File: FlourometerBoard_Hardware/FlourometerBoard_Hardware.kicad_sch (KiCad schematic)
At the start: 14 parts, among them J1 RJ45_LED_Shielded, J2 Conn_01x12_Pin, U1 Teensy4.1_DEV-16771, U2 OKI

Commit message: Boxed and Labeled Circuits
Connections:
- no-connect marks 5 -> 47
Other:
- note added: "Connectors"
- note added: "Ethernet"
- note added: "Hamamatsu Connections"
- note added: "LEDs"
- note added: "OKI"
- note added: "Teensy"
- moved on the sheet: C1, C2, C3, Conn1A, Conn1B, D1, D2, D3, J1, J2, R1, R2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

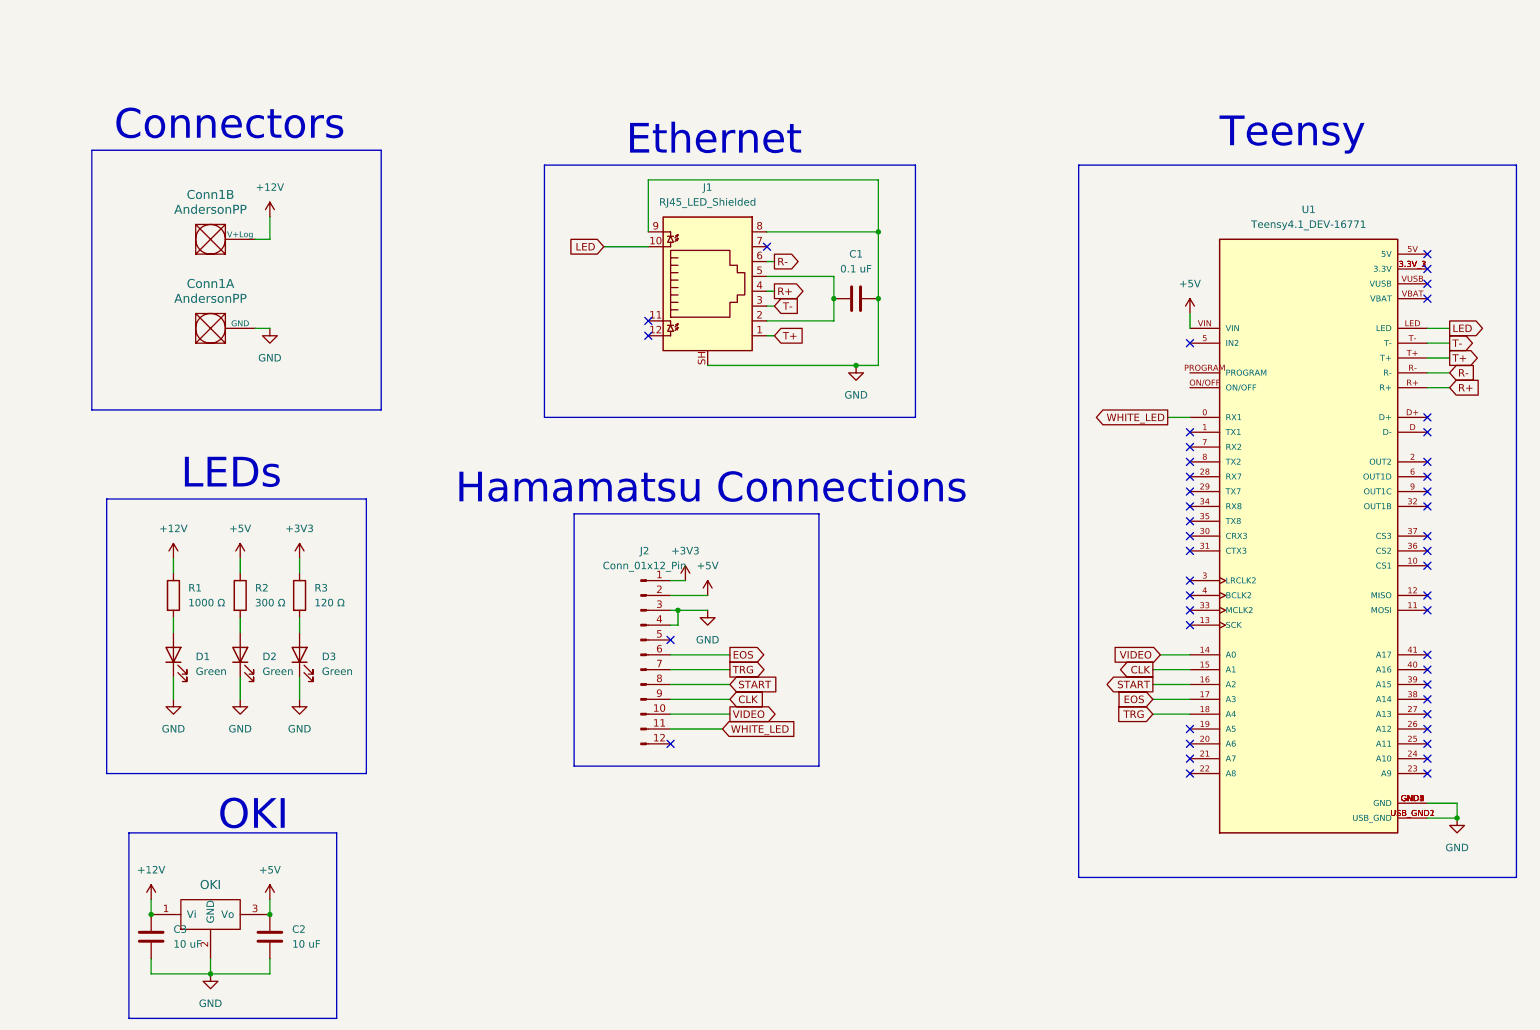
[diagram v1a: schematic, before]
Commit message: Update Board According to Schematic Review
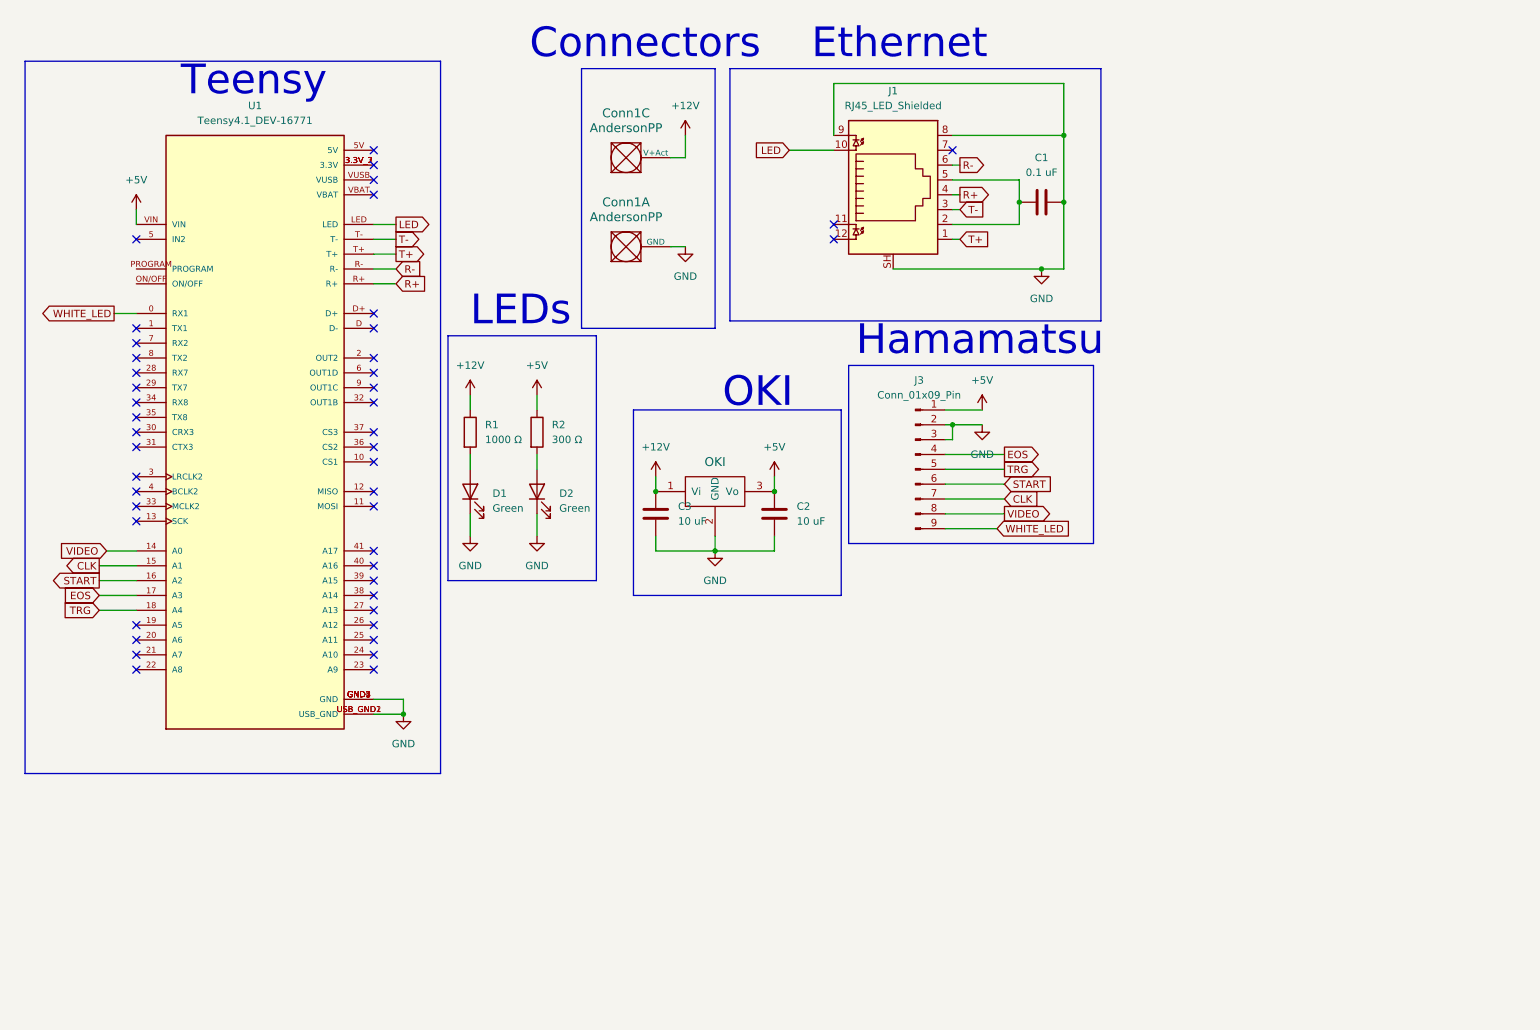
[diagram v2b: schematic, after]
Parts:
- removed unit 2 of Conn1
- removed D3: Green, symbol Device:LED
- removed J2: Conn_01x12_Pin, symbol Connector:Conn_01x12_Pin
- removed R3: 120 Ω, symbol Device:R
- added unit 3 of Conn1
- added J3: Conn_01x09_Pin, MRDT_Connectors:MOLEX_SL_09_Vertical, symbol Connector:Conn_01x09_Pin
- C1, C2, C3: footprint (none) -> Capacitor_SMD:C_0603_1608Metric_Pad1.08x0.95mm_HandSolder
- Conn1: footprint (none) -> MRDT_Connectors:Square_Anderson_2_H_Side_By_Side_PV
- D1, D2: footprint (none) -> LED_SMD:LED_0603_1608Metric_Pad1.05x0.95mm_HandSolder
- J1: footprint (none) -> MRDT_Connectors:RJ45_Teensy
- R1, R2: footprint (none) -> Resistor_SMD:R_0603_1608Metric_Pad0.98x0.95mm_HandSolder
- U1: footprint MODULE_DEV-16771 -> MRDT_Shields:Teensy_4_1_Ethernet
- U2: footprint (none) -> MRDT_Devices:OKI_Horizontal
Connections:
- net +12V: now also Conn1.3 (V+Act)
- net +5V: now also J3.1 (Pin_1)
- net CLK: now also J3.7 (Pin_7)
- net EOS: now also J3.4 (Pin_4)
- net GND: now also J3.2 (Pin_2), J3.3 (Pin_3)
- net START: now also J3.6 (Pin_6)
- net TRG: now also J3.5 (Pin_5)
- net VIDEO: now also J3.8 (Pin_8)
- net WHITE_LED: now also J3.9 (Pin_9)
- no-connect marks 47 -> 45
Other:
- note added: "Hamamatsu"
- note removed: "Hamamatsu Connections"
- moved on the sheet: C1, C2, C3, Conn1A, D1, D2, J1, R1, R2, U1

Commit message: Organized Schematic, Changed Anderson to V+Log
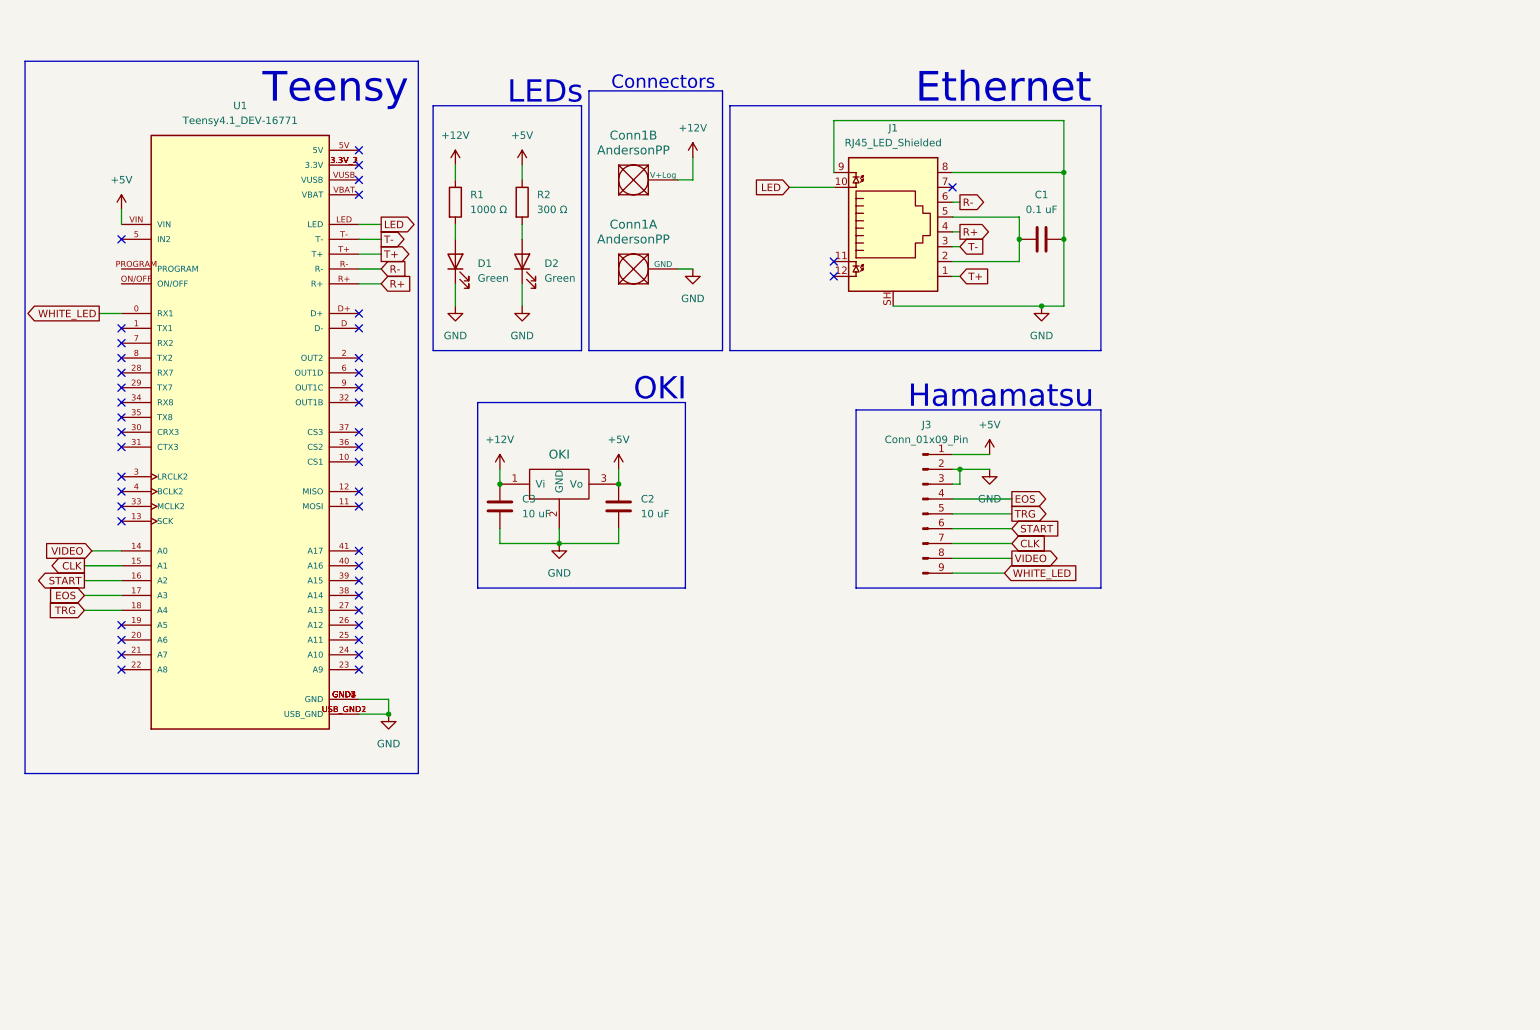
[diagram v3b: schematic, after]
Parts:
- removed unit 3 of Conn1
- added unit 2 of Conn1
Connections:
- net +12V: now also Conn1.2 (V+Log)
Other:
- moved on the sheet: C1, C2, C3, Conn1A, D1, D2, J1, J3, R1, R2, U1

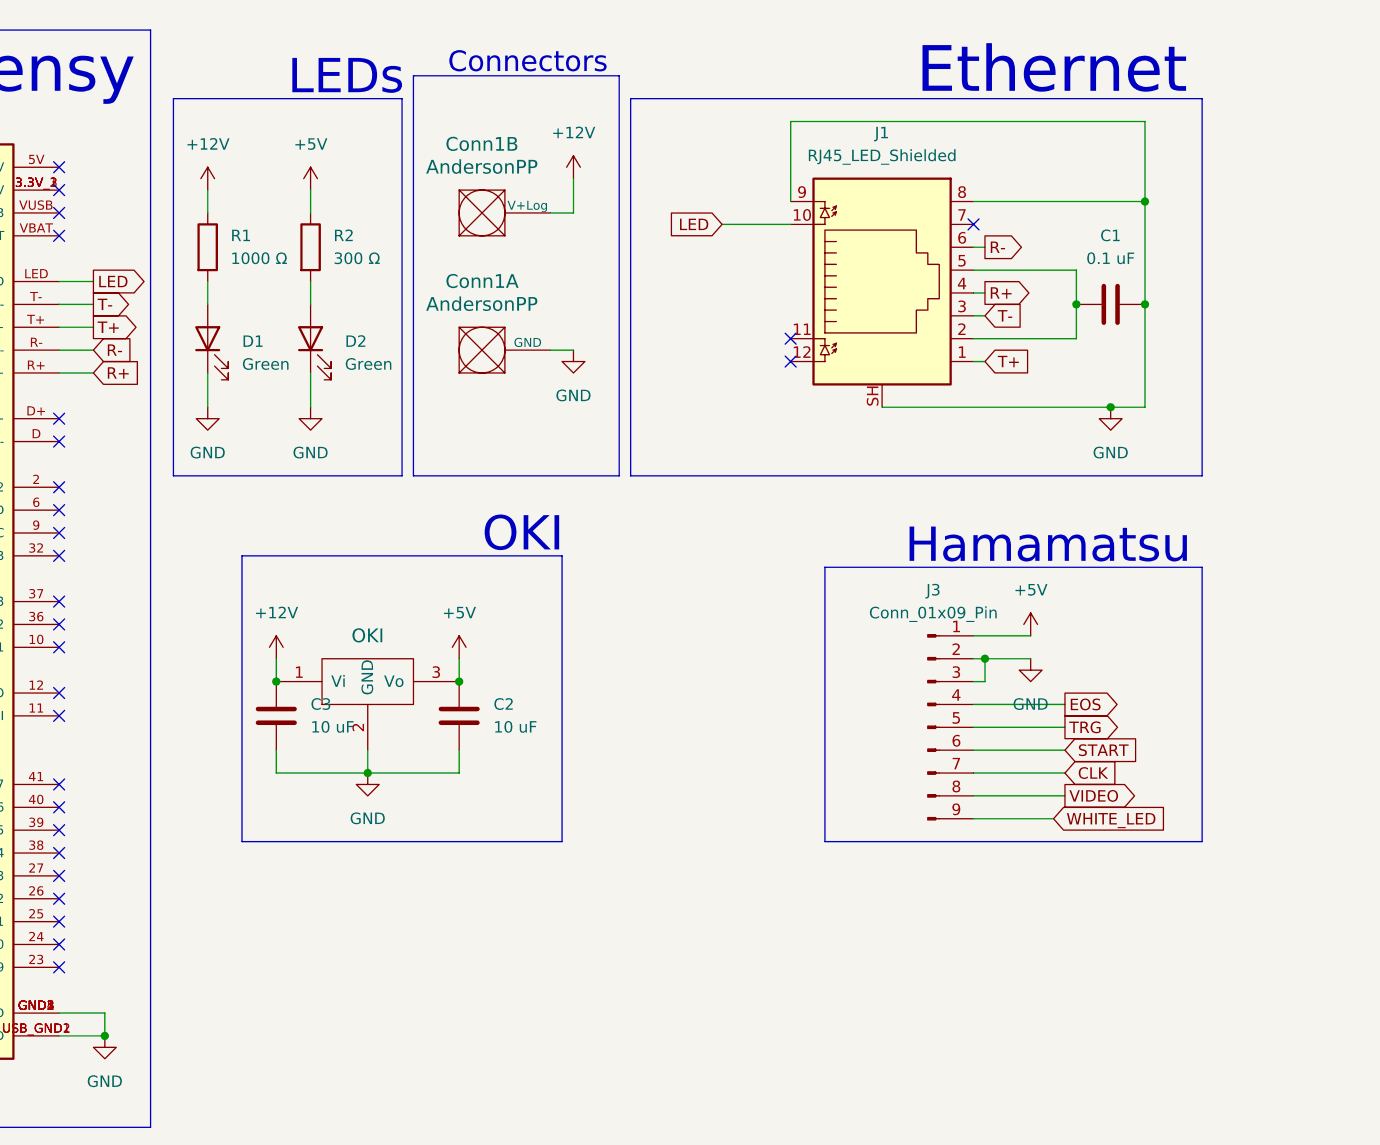
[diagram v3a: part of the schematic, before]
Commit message: Organized Schematic, added 12V to 3V3 converter
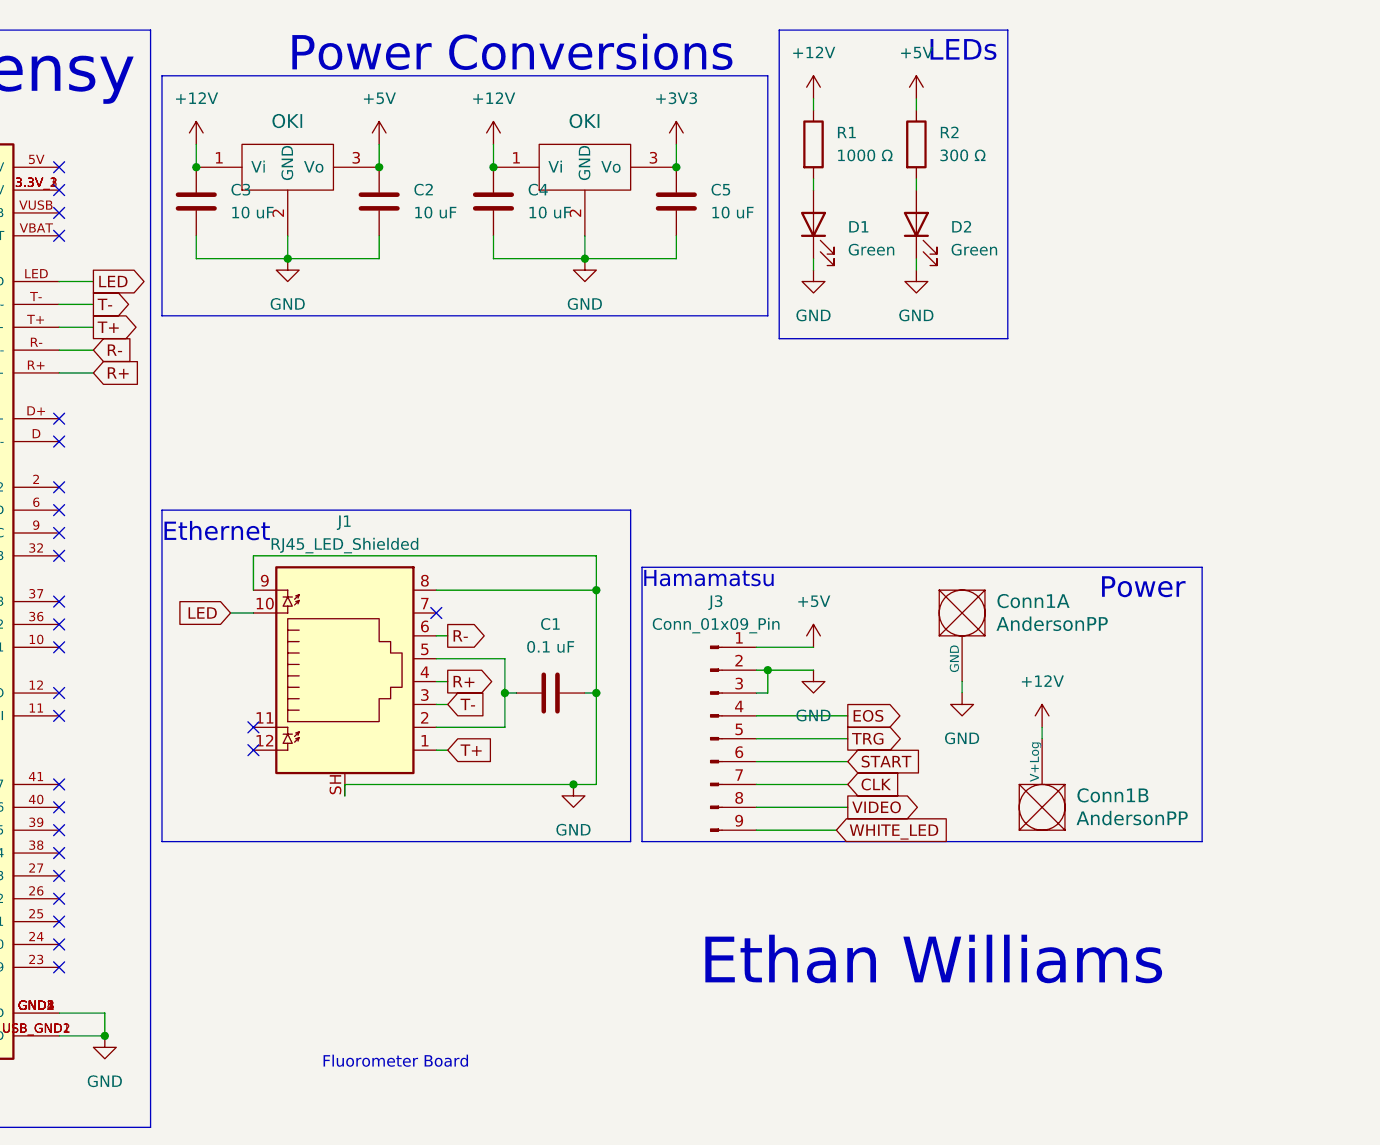
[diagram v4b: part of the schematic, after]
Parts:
- added C4, C5: 10 uF, Capacitor_SMD:C_0603_1608Metric_Pad1.08x0.95mm_HandSolder, symbol Device:C
- added U3: OKI, MRDT_Devices:OKI_Horizontal, symbol MRDT_Devices:OKI
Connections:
- net +12V: now also C4.1, U3.1 (Vi)
- net GND: now also C4.2, C5.2, U3.2 (GND)
- new net +3V3: C5.1, U3.3 (Vo)
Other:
- note added: "Ethan Williams"
- note added: "Fluorometer Board"
- note added: "Power"
- note added: "Power Conversions"
- note removed: "Connectors"
- note removed: "OKI"
- moved on the sheet: C1, C2, C3, Conn1A, Conn1B, D1, D2, J1, J3, R1, R2
